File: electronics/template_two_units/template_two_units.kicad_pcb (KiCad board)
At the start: 2 copper layers, 19 x 19 mm, 6 parts, among them J1 LEFT_TOP, J2 LEFT_BOT, J3 RIGHT_TOP, J4 RIGHT_BOT

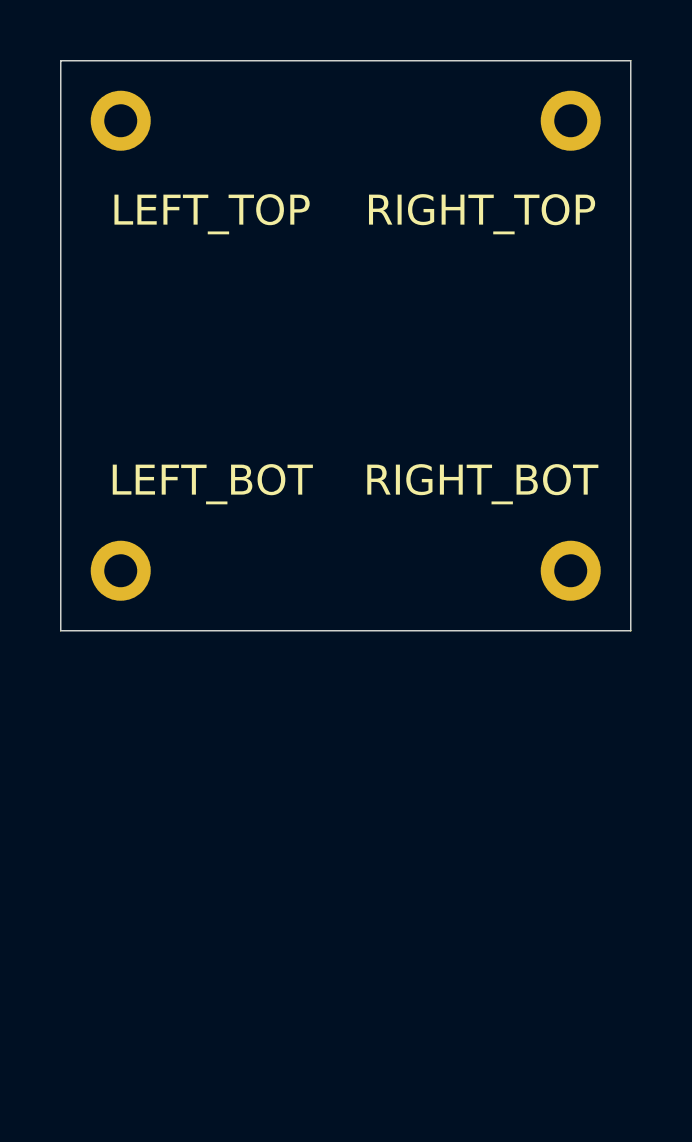
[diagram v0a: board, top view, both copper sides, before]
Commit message: template two units for kosmos modules
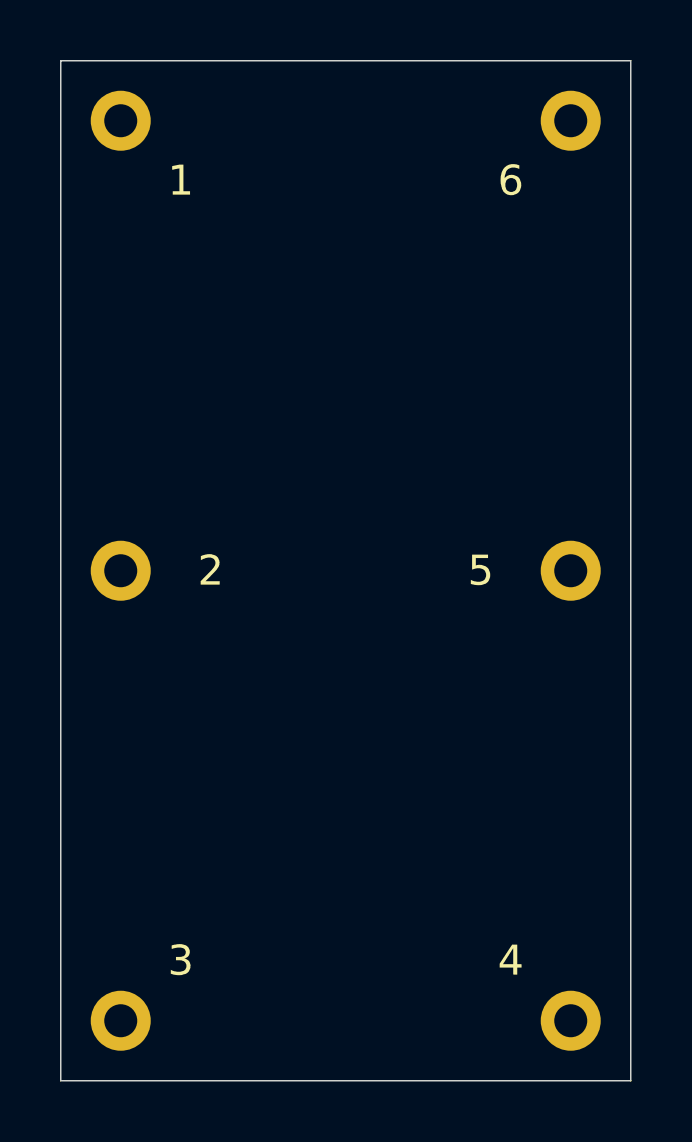
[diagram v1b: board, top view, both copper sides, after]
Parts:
- added J5: 5, mill-max:PC_pin_nail_head_6092, F.Cu at (157.0, 78.0)
- added J6: 6, mill-max:PC_pin_nail_head_6092, F.Cu at (157.0, 63.0)
- J1: value LEFT_TOP -> 1
- J2: value LEFT_BOT -> 2
- J3: value RIGHT_TOP -> 3
- J4: value RIGHT_BOT -> 4
- N1: value 20201118 -> 20201119
- moved J3 33.5 mm to (142.0, 93.0)
- moved J4 15.0 mm to (157.0, 93.0)
- moved N1 8.50 mm to (149.0, 82.0)
- moved N2 8.41 mm to (150.0, 78.0)
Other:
- board size 19 x 19 mm -> 19 x 34 mm
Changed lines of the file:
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@@
     (tracks 0)
     (zones 0)
-    (modules 6)
+    (modules 8)
     (nets 2)
   )
@@
     (add_net "Net-(J1-Pad1)")
   )
+  (module mill-max:PC_pin_nail_head_6092 (layer F.Cu)
+    (at 157 63)
+    (fp_text reference J6 (at -2 2) (layer F.Fab)
+      (effects (font (size 1 1) (thickness 0.15)))
+    )
+    (fp_text value 6 (at -2 2) (layer F.SilkS)
+      (effects (font (size 1 1) (thickness 0.15)))
+    )
+    (fp_circle (center 0 0) (end 1.3 0) (layer F.CrtYd) (width 0.025))
+    (fp_circle (center 0 0) (end 1.3 0) (layer B.CrtYd) (width 0.025))
+    (pad 1 thru_hole circle (at 0 0) (size 2 2) (drill 1.1) (layers *.Cu *.Mask)
+      (net 1 "Net-(J1-Pad1)"))
+  )
+  (module mill-max:PC_pin_nail_head_6092 (layer F.Cu)
+    (at 157 78)
+    (fp_text reference J5 (at -3 0) (layer F.Fab)
+      (effects (font (size 1 1) (thickness 0.15)))
+    )
+    (fp_text value 5 (at -3 0) (layer F.SilkS)
+      (effects (font (size 1 1) (thickness 0.15)))
+    )
+    (fp_circle (center 0 0) (end 1.3 0) (layer F.CrtYd) (width 0.025))
+    (fp_circle (center 0 0) (end 1.3 0) (layer B.CrtYd) (width 0.025))
+    (pad 1 thru_hole circle (at 0 0) (size 2 2) (drill 1.1) (layers *.Cu *.Mask)
+      (net 1 "Net-(J1-Pad1)"))
+  )
   (module mill-max:PC_pin_nail_head_6092 locked (layer F.Cu)
-    (at 157 78)
-    (fp_text reference J4 (at -3 0) (layer F.Fab)
-      (effects (font (size 1 1) (thickness 0.15)))
-    )
-    (fp_text value RIGHT_BOT (at -3 -3) (layer F.SilkS)
-      (effects (font (size 1 1) (thickness 0.15)))
-    )
-    (fp_circle (center 0 0) (end 1.3 0) (layer F.CrtYd) (width 0.025))
-    (fp_circle (center 0 0) (end 1.3 0) (layer B.CrtYd) (width 0.025))
+    (at 157 93)
+    (fp_text reference J4 (at -2 -2) (layer F.Fab)
+      (effects (font (size 1 1) (thickness 0.15)))
+    )
+    (fp_text value 4 (at -2 -2) (layer F.SilkS)
+      (effects (font (size 1 1) (thickness 0.15)))
+    )
+    (fp_circle (center 0 0) (end 1.3 0) (layer B.CrtYd) (width 0.025))
+    (fp_circle (center 0 0) (end 1.3 0) (layer F.CrtYd) (width 0.025))
     (pad 1 thru_hole circle (at 0 0) (size 2 2) (drill 1.1) (layers *.Cu *.Mask)
       (net 1 "Net-(J1-Pad1)"))
   )
   (module mill-max:PC_pin_nail_head_6092 locked (layer F.Cu)
-    (at 157 63)
-    (fp_text reference J3 (at -3 0) (layer F.Fab)
-      (effects (font (size 1 1) (thickness 0.15)))
-    )
-    (fp_text value RIGHT_TOP (at -3 3) (layer F.SilkS)
-      (effects (font (size 1 1) (thickness 0.15)))
-    )
-    (fp_circle (center 0 0) (end 1.3 0) (layer F.CrtYd) (width 0.025))
-    (fp_circle (center 0 0) (end 1.3 0) (layer B.CrtYd) (width 0.025))
+    (at 142 93)
+    (fp_text reference J3 (at 2 -2) (layer F.Fab)
+      (effects (font (size 1 1) (thickness 0.15)))
+    )
+    (fp_text value 3 (at 2 -2) (layer F.SilkS)
+      (effects (font (size 1 1) (thickness 0.15)))
+    )
+    (fp_circle (center 0 0) (end 1.3 0) (layer B.CrtYd) (width 0.025))
+    (fp_circle (center 0 0) (end 1.3 0) (layer F.CrtYd) (width 0.025))
     (pad 1 thru_hole circle (at 0 0) (size 2 2) (drill 1.1) (layers *.Cu *.Mask)
       (net 1 "Net-(J1-Pad1)"))
@@
       (effects (font (size 1 1) (thickness 0.15)))
     )
-    (fp_text value LEFT_BOT (at 3 -3) (layer F.SilkS)
-      (effects (font (size 1 1) (thickness 0.15)))
-    )
-    (fp_circle (center 0 0) (end 1.3 0) (layer F.CrtYd) (width 0.025))
-    (fp_circle (center 0 0) (end 1.3 0) (layer B.CrtYd) (width 0.025))
+    (fp_text value 2 (at 3 0) (layer F.SilkS)
+      (effects (font (size 1 1) (thickness 0.15)))
+    )
+    (fp_circle (center 0 0) (end 1.3 0) (layer B.CrtYd) (width 0.025))
+    (fp_circle (center 0 0) (end 1.3 0) (layer F.CrtYd) (width 0.025))
     (pad 1 thru_hole circle (at 0 0) (size 2 2) (drill 1.1) (layers *.Cu *.Mask)
       (net 1 "Net-(J1-Pad1)"))
@@
   (module mill-max:PC_pin_nail_head_6092 locked (layer F.Cu)
     (at 142 63)
-    (fp_text reference J1 (at 3 0) (layer F.Fab)
-      (effects (font (size 1 1) (thickness 0.15)))
-    )
-    (fp_text value LEFT_TOP (at 3 3) (layer F.SilkS)
-      (effects (font (size 1 1) (thickness 0.15)))
-    )
-    (fp_circle (center 0 0) (end 1.3 0) (layer F.CrtYd) (width 0.025))
-    (fp_circle (center 0 0) (end 1.3 0) (layer B.CrtYd) (width 0.025))
+    (fp_text reference J1 (at 2 2) (layer F.Fab)
+      (effects (font (size 1 1) (thickness 0.15)))
+    )
+    (fp_text value 1 (at 2 2) (layer F.SilkS)
+      (effects (font (size 1 1) (thickness 0.15)))
+    )
+    (fp_circle (center 0 0) (end 1.3 0) (layer B.CrtYd) (width 0.025))
+    (fp_circle (center 0 0) (end 1.3 0) (layer F.CrtYd) (width 0.025))
     (pad 1 thru_hole circle (at 0 0) (size 2 2) (drill 1.1) (layers *.Cu *.Mask)
       (net 1 "Net-(J1-Pad1)"))
   )
   (module Symbol:OSHW-Symbol_6.7x6mm_SilkScreen (layer B.Cu)
-    (at 149.7 69.6 180)
+    (at 150 78 180)
     (descr "Open Source Hardware Symbol")
     (tags "Logo Symbol OSHW")
@@
   )
   (module SquantorLabels:Label_Generic (layer B.Cu)
-    (at 149.1 73.5)
+    (at 149 82)
     (descr "Label for general purpose use")
     (tags Label)
@@
       (effects (font (size 1 1) (thickness 0.15)) (justify mirror))
     )
-    (fp_text value 20201118 (at 0.8 0.1) (layer B.SilkS)
+    (fp_text value 20201119 (at 0.8 0.1) (layer B.SilkS)
       (effects (font (size 0.8 0.8) (thickness 0.15)) (justify mirror))
     )
@@
   )
   (gr_line (start 159 61) (end 140 61) (layer Edge.Cuts) (width 0.05))
-  (gr_line (start 159 61) (end 159 80) (layer Edge.Cuts) (width 0.05))
-  (gr_line (start 140 80) (end 159 80) (layer Edge.Cuts) (width 0.05))
-  (gr_line (start 140 80) (end 140 61) (layer Edge.Cuts) (width 0.05))
+  (gr_line (start 159 61) (end 159 95) (layer Edge.Cuts) (width 0.05))
+  (gr_line (start 140 95) (end 159 95) (layer Edge.Cuts) (width 0.05))
+  (gr_line (start 140 95) (end 140 61) (layer Edge.Cuts) (width 0.05))
 )
